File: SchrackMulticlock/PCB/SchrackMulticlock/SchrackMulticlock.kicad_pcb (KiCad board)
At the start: 4 copper layers, 140 x 59.5 mm, 83 parts, among them J1 TYPE-C-31-M-12 (USB C CONN), Q1 Q_PMOS, SW1 SW_SPST, SW2 SW_Push, SW3 SW_Push, SW4 SW_Push, SW5 SW_Push, SW6 SW_Push, SW7 SW_Push, SW8 SW_Push, SW9 SW_Push, U1 LM1117DT-3.3, U2 LDD080AUE-101A, U3 LDD080AUE-101A, U4 LDD080AUE-101A, U5 MAX7219, U6 ESP32-S3-WROOM-2, U7 USBLC6-2SC6, U8 74HC14

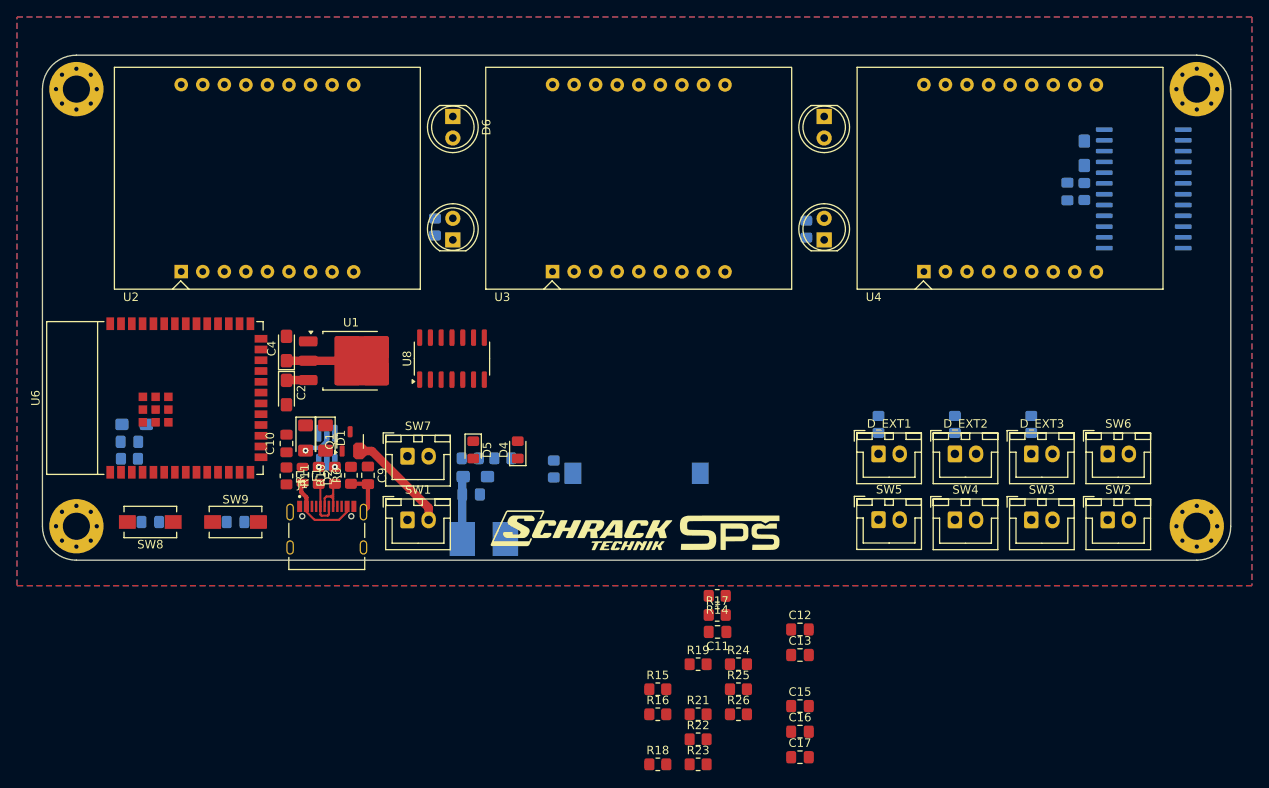
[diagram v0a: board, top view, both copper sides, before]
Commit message: SchrackMulticlock PCB final routing
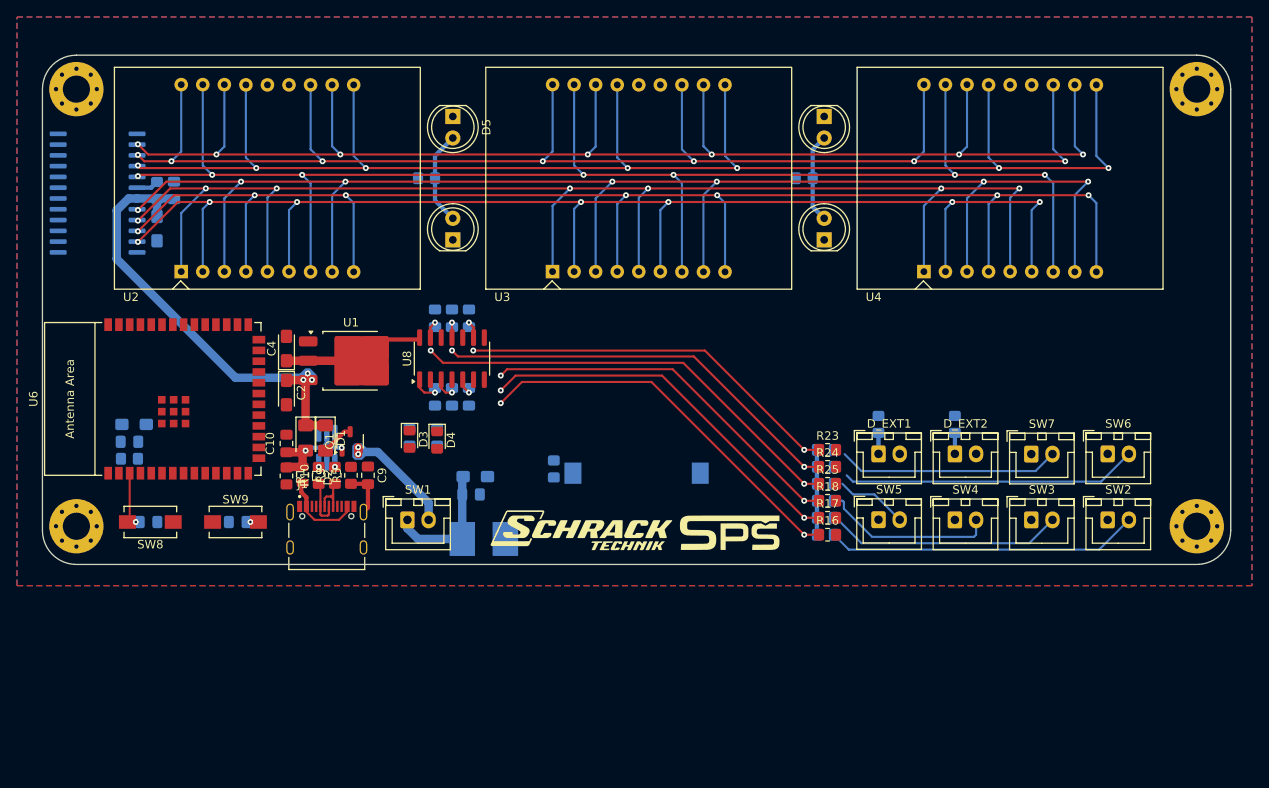
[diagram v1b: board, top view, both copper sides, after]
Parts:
- removed D_EXT3: Conn_01x02_Pin, Connector_JST:JST_XH_B2B-XH-A_1x02_P2.50mm_Vertical
- removed the R5 at (239.3, 102.3)
- removed the R9 at (173.2, 106.3)
- added R7: 220R, Resistor_SMD:R_0805_2012Metric_Pad1.20x1.40mm_HandSolder, B.Cu at (166.1, 103.8)
- C11, C12, C13, C15, C16, C17: moved to B.Cu
- R13: renamed from R14; moved to B.Cu
- R14: renamed from R15; moved to B.Cu
- R15: renamed from R16; moved to B.Cu
- R20: renamed from R21; moved to B.Cu
- R21: renamed from R22; moved to B.Cu
- R22: renamed from R23; moved to B.Cu
- U6: value ESP32-S3-WROOM-2 -> ESP32-S3-WROOM-1; footprint PCM_Espressif:ESP32-S3-WROOM-2 -> PCM_Espressif:ESP32-S3-WROOM-1
- moved U5 123.3 mm to (129.3, 75.1), turned to 0 degrees
- moved C5 109.6 mm to (136.3, 79.3), turned to -90 degrees
- moved R2 109.3 mm to (136.3, 74.8), turned to 90 degrees
- moved C6 105.3 mm to (138.3, 74.8), turned to 90 degrees
- moved SW7 73.5 mm to (239.3, 105.8)
- moved C17 66.0 mm to (171.1, 89.8), turned to -90 degrees
- moved C16 62.4 mm to (173.1, 89.8), turned to -90 degrees
- moved C13 58.5 mm to (169.1, 89.8), turned to -90 degrees
- moved C15 54.9 mm to (171.1, 99.1), turned to 90 degrees
- moved C12 47.7 mm to (173.1, 99.1), turned to 90 degrees
- moved C11 43.3 mm to (169.1, 99.1), turned to 90 degrees
- moved R22 36.3 mm to (215.1, 109.3), turned to 180 degrees
- moved R21 35.4 mm to (215.1, 107.3), turned to 180 degrees
- moved R17 35.3 mm to (215.3, 113.3)
- moved R20 34.6 mm to (215.1, 105.3), turned to 180 degrees
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- renumbered D4 to D3, D5 to D4, D6 to D5, D7 to D6, D8 to D7, D9 to D8, R11 to R10, R12 to R11, R13 to R12, R17 to R16, R18 to R17, R19 to R18, R20 to R19, R24 to R23, R25 to R24, R26 to R25, R6 to R5, R7 to R6, R10 to R9
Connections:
- net /MECHANICS/BT2 renamed /MECHANICS/STRT
- net /MECHANICS/TP renamed /MECHANICS/TU
- D3 pad 1: Net-(D4-K) -> GND
- D3 pad 2: +3V3 -> Net-(D3-A)
- D4 pad 1: Net-(D5-K) -> GND
- D4 pad 2: VBATT_OUT -> Net-(D4-A)
- R22 pad 1: AUX -> /MECHANICS/RST
- R25 pad 2: AUX -> /MECHANICS/RST
- R8 pad 1: Net-(D4-K) -> VBATT_OUT
- R8 pad 2: GND -> Net-(D4-A)
- SW7 pad 2: AUX -> /MECHANICS/RST
- U6 pad 12: unconnected-(U6-IO8-Pad12) -> AUX2
- U6 pad 17: unconnected-(U6-IO9-Pad17) -> AUX1
- U6 pad 18: unconnected-(U6-IO10-Pad18) -> TIME_DOWN
- U6 pad 19: unconnected-(U6-IO11-Pad19) -> RESET
- U6 pad 20: unconnected-(U6-IO12-Pad20) -> TIME_UP
- U6 pad 21: unconnected-(U6-IO13-Pad21) -> DIGIT_SELECT
- U6 pad 22: unconnected-(U6-IO14-Pad22) -> MODE
- U6 pad 28: (no net) -> MOSI
- U6 pad 29: (no net) -> CLK
- U6 pad 30: (no net) -> ~{CS}
- U6 pad 4: unconnected-(U6-IO4-Pad4) -> COLON_1
- U6 pad 5: unconnected-(U6-IO5-Pad5) -> COLON_2
- U6 pad 6: unconnected-(U6-IO6-Pad6) -> BZ1_PWM
- U6 pad 7: unconnected-(U6-IO7-Pad7) -> AUX3
- U6 pad 8: unconnected-(U6-IO15-Pad8) -> START/STOP
- U8 pad 10: AUX -> RESET
- U8 pad 4: BTN2 -> START/STOP
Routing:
- net SEG_C: track 0.00 -> 181.6 mm, vias 0 -> 7
- net SEG_B: track 0.00 -> 176.7 mm, vias 0 -> 7
- net SEG_G: track 0.00 -> 175.8 mm, vias 0 -> 7
- net SEG_DP: track 0.00 -> 170.4 mm, vias 0 -> 7
- net SEG_E: track 0.00 -> 168.6 mm, vias 0 -> 7
- net SEG_F: track 0.00 -> 167.0 mm, vias 0 -> 7
- net SEG_A: track 0.00 -> 163.6 mm, vias 0 -> 7
- net SEG_D: track 0.00 -> 159.7 mm, vias 0 -> 7
- net Net-(C17-Pad2): track 0.00 -> 54.6 mm, vias 0 -> 3
- net Net-(C16-Pad2): track 0.00 -> 51.5 mm, vias 0 -> 3
- net +5V: track 2.53 -> 53.8 mm, vias 0 -> 3
- net Net-(C11-Pad2): track 0.00 -> 49.5 mm, vias 0 -> 3
- net Net-(C15-Pad2): track 0.00 -> 48.6 mm, vias 0 -> 3
- net Net-(C12-Pad2): track 0.00 -> 47.5 mm, vias 0 -> 3
- net Net-(C13-Pad2): track 0.00 -> 46.8 mm, vias 0 -> 3
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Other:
- board size 140 x 59.5 mm -> 140 x 60 mm

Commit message: Multiclock a lot of routing and layout
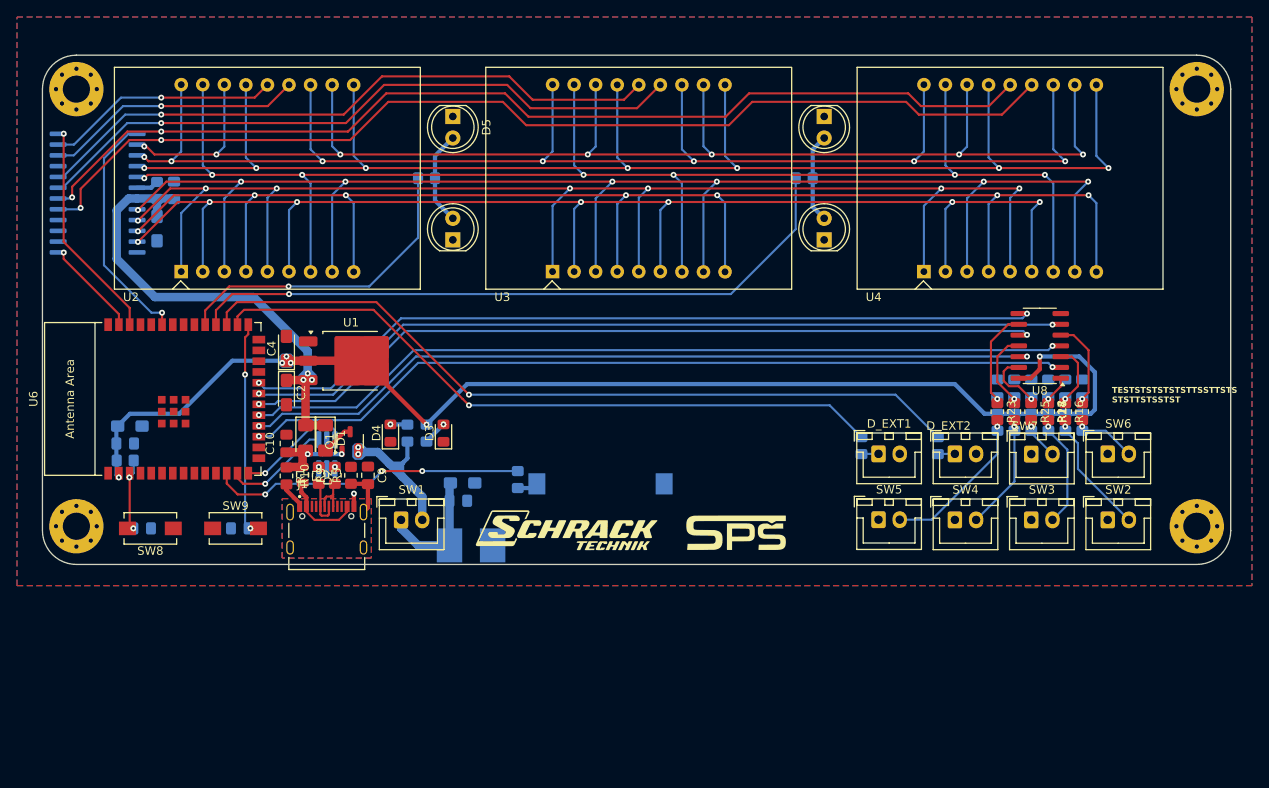
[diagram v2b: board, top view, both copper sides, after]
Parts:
- moved C11 74.3 mm to (243.3, 98.1), turned to -90 degrees
- moved C16 72.7 mm to (245.3, 98.1)
- moved U8 69.3 mm to (240.3, 93.1), turned to 180 degrees
- moved C13 68.7 mm to (237.3, 98.1)
- moved C17 68.7 mm to (239.3, 98.1)
- moved C12 68.3 mm to (241.3, 98.1), turned to -90 degrees
- moved C15 64.3 mm to (235.3, 98.1), turned to -90 degrees
- moved R16 31.5 mm to (243.3, 100.8), turned to -90 degrees
- moved R13 31.2 mm to (243.3, 102.1), turned to 90 degrees
- moved R21 30.7 mm to (245.3, 102.1), turned to 90 degrees
- moved R24 30.7 mm to (245.3, 100.8), turned to -90 degrees
- moved R17 28.8 mm to (241.3, 100.8), turned to -90 degrees
- moved R14 28.6 mm to (241.3, 102.1), turned to 90 degrees
- moved R25 25.4 mm to (239.3, 100.8), turned to -90 degrees
- moved R22 25.3 mm to (239.3, 102.1), turned to 90 degrees
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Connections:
- R20 pad 1: /MECHANICS/STRT -> /MECHANICS/RST
- R22 pad 1: /MECHANICS/RST -> /MECHANICS/STRT
- R23 pad 2: /MECHANICS/STRT -> /MECHANICS/RST
- R25 pad 2: /MECHANICS/RST -> /MECHANICS/STRT
- SW5 pad 2: /MECHANICS/STRT -> /MECHANICS/RST
- SW7 pad 2: /MECHANICS/RST -> /MECHANICS/STRT
- U5 pad 10: unconnected-(U5-DIG_5-Pad10) -> DIG_1
- U5 pad 11: unconnected-(U5-DIG_1-Pad11) -> DIG_0
- U5 pad 5: unconnected-(U5-DIG_6-Pad5) -> DIG_3
- U5 pad 6: unconnected-(U5-DIG_2-Pad6) -> DIG_2
- U5 pad 7: unconnected-(U5-DIG_3-Pad7) -> DIG_5
- U5 pad 8: unconnected-(U5-DIG_7-Pad8) -> DIG_4
- U6 pad 12: AUX2 -> BZ1_PWM
- U6 pad 17: AUX1 -> TIME_UP
- U6 pad 18: TIME_DOWN -> START/STOP
- U6 pad 19: RESET -> MODE
- U6 pad 20: TIME_UP -> TIME_DOWN
- U6 pad 22: MODE -> RESET
- U6 pad 28: MOSI -> AUX1
- U6 pad 29: CLK -> AUX2
- U6 pad 30: ~{CS} -> COLON_2
- U6 pad 31: unconnected-(U6-IO38-Pad31) -> COLON_1
- U6 pad 35: unconnected-(U6-IO42-Pad35) -> CLK
- U6 pad 38: unconnected-(U6-IO2-Pad38) -> ~{CS}
- U6 pad 39: unconnected-(U6-IO1-Pad39) -> MOSI
- U6 pad 4: COLON_1 -> unconnected-(U6-IO4-Pad4)
- U6 pad 5: COLON_2 -> unconnected-(U6-IO5-Pad5)
- U6 pad 6: BZ1_PWM -> unconnected-(U6-IO6-Pad6)
- U6 pad 7: AUX3 -> unconnected-(U6-IO7-Pad7)
- U6 pad 8: START/STOP -> unconnected-(U6-IO15-Pad8)
- U8 pad 1: Net-(C11-Pad2) -> Net-(C12-Pad2)
- U8 pad 10: RESET -> TIME_DOWN
- U8 pad 11: Net-(C17-Pad2) -> Net-(C13-Pad2)
- U8 pad 12: TIME_DOWN -> START/STOP
- U8 pad 13: Net-(C13-Pad2) -> Net-(C17-Pad2)
- U8 pad 2: MODE -> TIME_UP
- U8 pad 3: Net-(C15-Pad2) -> Net-(C11-Pad2)
- U8 pad 4: START/STOP -> MODE
- U8 pad 5: Net-(C12-Pad2) -> Net-(C16-Pad2)
- U8 pad 6: TIME_UP -> DIGIT_SELECT
- U8 pad 8: DIGIT_SELECT -> RESET
- U8 pad 9: Net-(C16-Pad2) -> Net-(C15-Pad2)
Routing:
- net DIG_3: track 0.00 -> 125.6 mm, vias 0 -> 2
- net +3V3: track 24.2 -> 146.8 mm, vias 0 -> 6
- net DIG_2: track 0.00 -> 122.0 mm, vias 0 -> 2
- net TIME_UP: track 0.00 -> 98.3 mm, vias 0 -> 2
- net DIGIT_SELECT: track 0.00 -> 98.0 mm, vias 0 -> 2
- net MODE: track 0.00 -> 97.9 mm, vias 0 -> 2
- net RESET: track 0.00 -> 95.4 mm, vias 0 -> 2
- net TIME_DOWN: track 0.00 -> 95.2 mm, vias 0 -> 2
- net START/STOP: track 0.00 -> 94.9 mm, vias 0 -> 2
- net AUX2: track 0.00 -> 92.8 mm, vias 0 -> 1
- net AUX1: track 0.00 -> 81.0 mm, vias 0 -> 1
- net COLON_2: track 0.00 -> 80.0 mm, vias 0 -> 1
- net DIG_5: track 0.00 -> 78.2 mm, vias 0 -> 1
- net DIG_4: track 0.00 -> 75.2 mm, vias 0 -> 1
- net Net-(C17-Pad2): track 54.6 -> 7.68 mm, vias 3 -> 1
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- added copper zone on B.Cu, net /CONNECTIVITY/SHLD
- added copper zone on F.Cu, net /CONNECTIVITY/SHLD
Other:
- board text added: "TESTSTSTSTSTSTTSSTTSTS STSTTSTSSTST"

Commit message: Multiclock silkscreen updafe
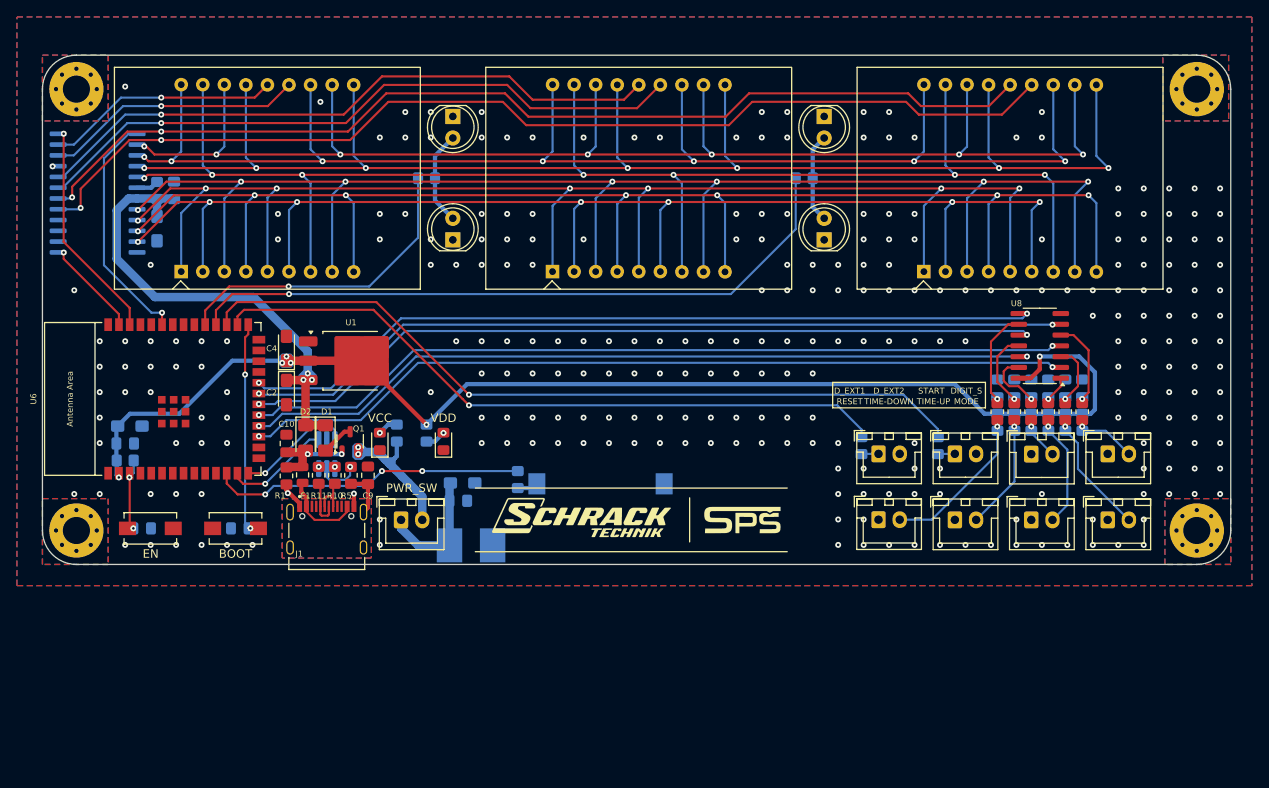
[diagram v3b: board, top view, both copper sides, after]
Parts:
- added TP3: TestPoint, sumec_graphic:BRAND_BERSERK, B.Cu at (221.0, 96.8)
- added TP4: TestPoint, sumec_graphic:BRAND_BERSERK_SOLDER, B.Cu at (212.6, 107.1)
- added TP4: TestPoint, sumec_graphic:BRAND_BERSERK_SOLDER, B.Cu at (252.2, 66.2)
- moved TP2 2.30 mm to (186.3, 113.3)
- moved TP1 1.68 mm to (205.1, 113.3)
- moved D4 1.59 mm to (162.6, 104.3)
- moved R8 1.25 mm to (164.6, 103.4)
- moved D3 0.97 mm to (170.1, 104.3)
- moved H3 0.50 mm to (126.8, 114.8)
- moved H4 0.50 mm to (258.8, 114.8)
- renumbered D5 to D6, D6 to D7, D7 to D8, D8 to D9, R9 to R10, R10 to R11, R11 to R12, R12 to R13, R13 to R14, R14 to R15, R15 to R16, R16 to R17, R17 to R18, R18 to R19, R19 to R20, R20 to R21, R21 to R22, R22 to R23, R23 to R24, R24 to R25, R25 to R26
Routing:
- net GND: track 4.74 -> 9.85 mm, vias 1 -> 274
- net VBATT_OUT: track 20.8 -> 18.8 mm
- net Net-(D4-A): track 2.05 -> 2.65 mm
- net AUX2: track 92.8 -> 93.4 mm
- net AUX1: track 81.0 -> 81.6 mm
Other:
- board text added: "BOOT"
- board text added: "DIGIT_S"
- board text added: "D_EXT1"
- board text added: "D_EXT2"
- board text added: "EN"
- board text added: "MADE BY BISMARX"
- board text added: "MODE"
- board text added: "PWR_SW"
- board text added: "RESET"
- board text added: "START"
- board text added: "TIME-DOWN"
- board text added: "TIME-UP"
- board text added: "VCC"
- board text added: "VDD"
- board text removed: "TESTSTSTSTSTSTTSSTTSTS STSTTSTSSTST"

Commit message: PCB order plotting
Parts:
- removed the TP4 at (212.6, 107.1)
- TP4: footprint sumec_graphic:BRAND_BERSERK_SOLDER -> sumec_graphic:BOCCHI_IMG
- moved TP4 125.4 mm to (132.2, 102.5), turned to 90 degrees
- moved TP3 43.5 mm to (251.5, 65.7), turned to -135 degrees
- moved R3 3.40 mm to (221.3, 102.1)
- moved R4 3.40 mm to (230.3, 102.1)
- moved TP2 0.25 mm to (186.3, 113.6)
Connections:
- R8 pad 1: VBATT_OUT -> +5V
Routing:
- net +5V: track 55.5 -> 65.9 mm, vias 3 -> 4
- net VBATT_OUT: track 18.8 -> 13.7 mm
- net Net-(D_EXT2-Pin_1): track 2.01 -> 2.73 mm
- net Net-(D_EXT1-Pin_1): track 2.01 -> 2.73 mm
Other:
- board text added: "BOCCHI :3"
